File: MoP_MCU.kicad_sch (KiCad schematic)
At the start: 4 parts, among them J3 CN7, J4 CN10

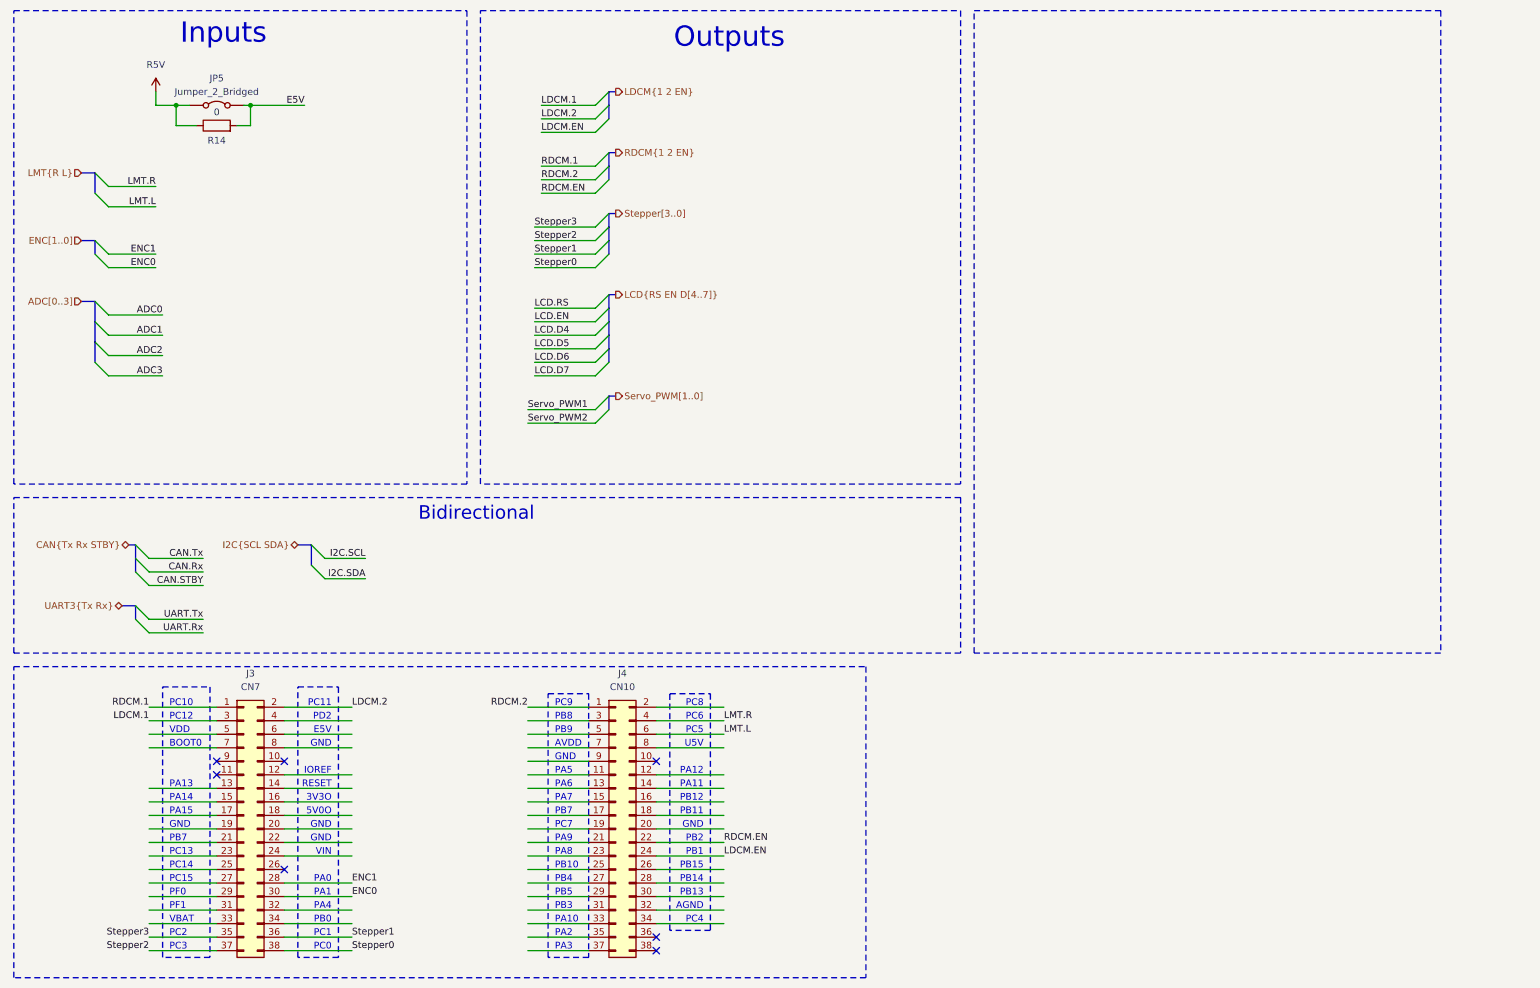
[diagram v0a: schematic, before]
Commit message: changed ref designators to be consistent accross sheets
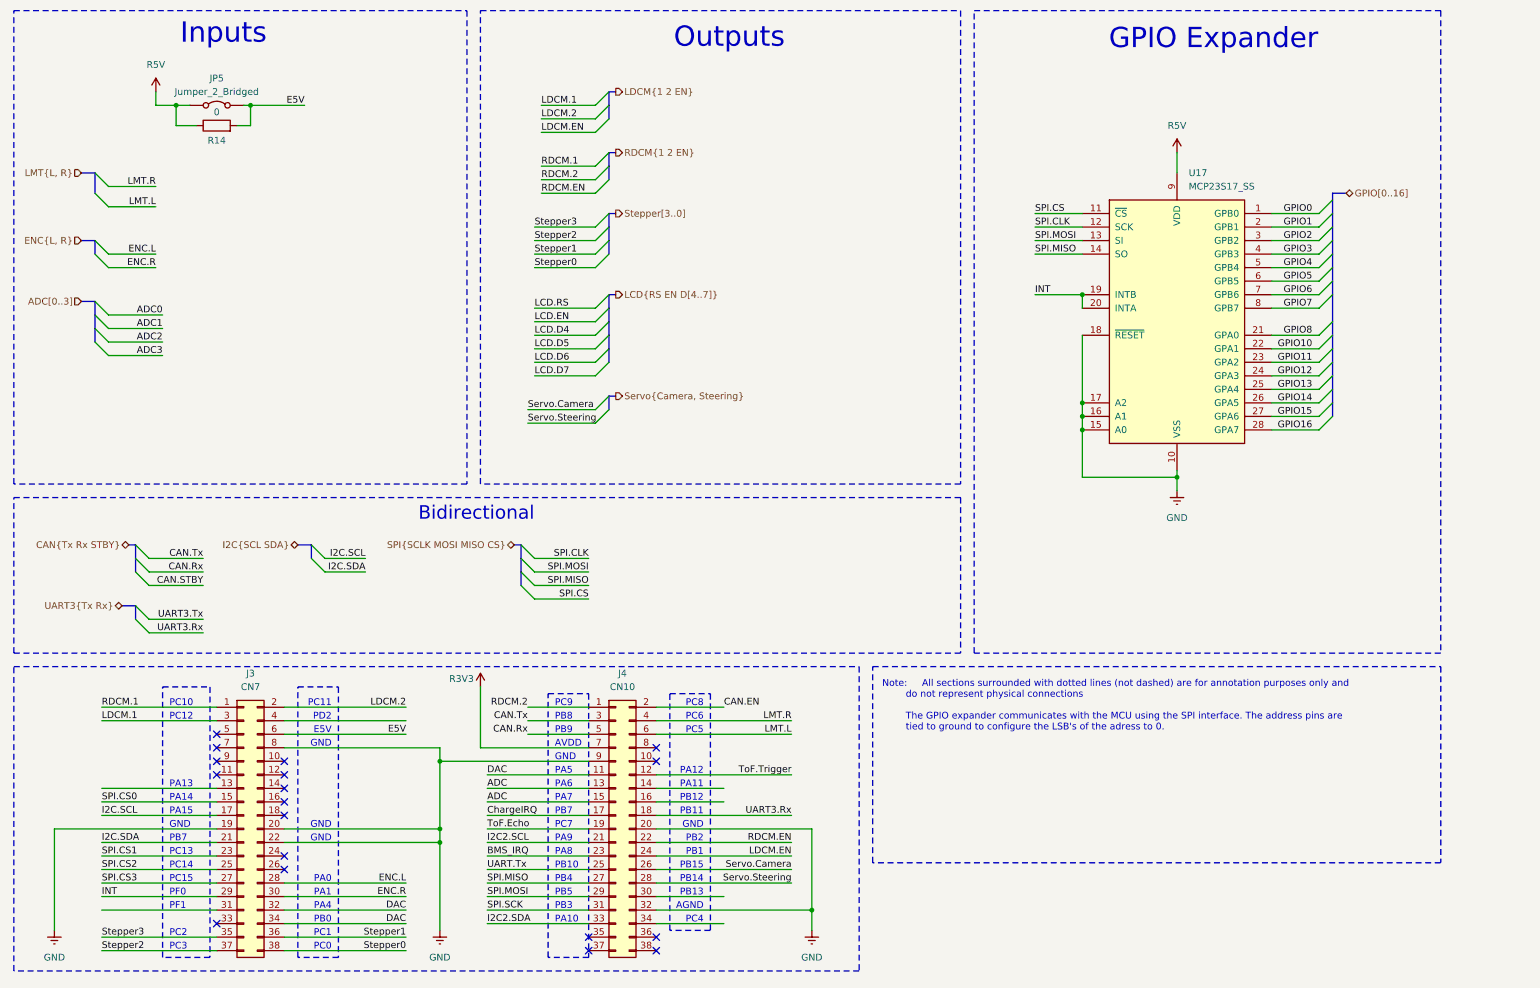
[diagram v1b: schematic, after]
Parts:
- added U17: MCP23S17_SS, Package_SO:SSOP-28_5.3x10.2mm_P0.65mm, symbol Interface_Expansion:MCP23S17_SS
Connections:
- net CAN.Rx: now also J4.5 (Pin_5)
- net CAN.Tx: now also J4.3 (Pin_3)
- net E5V: now also J3.6 (Pin_6)
- net I2C.SCL: now also J3.17 (Pin_17)
- net I2C.SDA: now also J3.21 (Pin_21)
- net R5V: now also U17.9 (VDD)
- net UART.Tx: now also J4.25 (Pin_25)
- net SPI.CS0: now reaches J3.15 (Pin_15)
- net GND: now reaches J3.19 (Pin_19)
- net GND: now also J3.20 (Pin_20), J3.22 (Pin_22), J3.8 (Pin_8), J4.20 (Pin_20), J4.32 (Pin_32), J4.9 (Pin_9), U17.10 (VSS), U17.15 (A0), U17.16 (A1), U17.17 (A2), U17.18 (~{RESET})
- net SPI.CS1: now reaches J3.23 (Pin_23)
- net SPI.CS2: now reaches J3.25 (Pin_25)
- net SPI.CS3: now reaches J3.27 (Pin_27)
- net INT: now reaches J3.29 (Pin_29)
- net INT: now also U17.19 (INTB), U17.20 (INTA)
- net DAC: now reaches J3.32 (Pin_32)
- net DAC: now also J3.34 (Pin_34), J4.11 (Pin_11)
- net ToF.Trigger: now reaches J4.12 (Pin_12)
- net ADC: now reaches J4.13 (Pin_13)
- net ADC: now also J4.15 (Pin_15)
- net ChargeIRQ: now reaches J4.17 (Pin_17)
- net UART3.Rx: now reaches J4.18 (Pin_18)
- net ToF.Echo: now reaches J4.19 (Pin_19)
- net CAN.EN: now reaches J4.2 (Pin_2)
- net I2C2.SCL: now reaches J4.21 (Pin_21)
- net BMS_IRQ: now reaches J4.23 (Pin_23)
- net Servo.Camera: now reaches J4.26 (Pin_26)
- net SPI.MISO: now reaches J4.27 (Pin_27)
- net SPI.MISO: now also U17.14 (SO)
- net Servo.Steering: now reaches J4.28 (Pin_28)
- net SPI.MOSI: now reaches J4.29 (Pin_29)
- net SPI.MOSI: now also U17.13 (SI)
- net SPI.SCK: now reaches J4.31 (Pin_31)
- net I2C2.SDA: now reaches J4.33 (Pin_33)
- net R3V3: now reaches J4.7 (Pin_7)
- net ENC0 renamed ENC.R
- net ENC1 renamed ENC.L
- new net GPIO0: U17.1 (GPB0)
- new net GPIO1: U17.2 (GPB1)
- new net GPIO10: U17.22 (GPA1)
- new net GPIO11: U17.23 (GPA2)
- new net GPIO12: U17.24 (GPA3)
- new net GPIO13: U17.25 (GPA4)
- new net GPIO14: U17.26 (GPA5)
- new net GPIO15: U17.27 (GPA6)
- new net GPIO16: U17.28 (GPA7)
- new net GPIO2: U17.3 (GPB2)
- new net GPIO3: U17.4 (GPB3)
- new net GPIO4: U17.5 (GPB4)
- new net GPIO5: U17.6 (GPB5)
- new net GPIO6: U17.7 (GPB6)
- new net GPIO7: U17.8 (GPB7)
- new net GPIO8: U17.21 (GPA0)
- new net SPI.CLK: U17.12 (SCK)
- new net SPI.CS: U17.11 (~{CS})
- no-connect marks 7 -> 18
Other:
- note added: "GPIO Expander"
- note added: "Note: All sections surrounded with dotted lines (not dashed) are for annotation purposes only and do not represent physical connections The GPIO expander communicates with the MCU using the SPI interface. The address pins are tied to ground to configure the LSB's of the adress to 0."
- note removed: "3V3O"
- note removed: "5V0O"
- note removed: "BOOT0"
- note removed: "IOREF"
- note removed: "PA2"
- note removed: "PA3"
- note removed: "RESET"
- note removed: "U5V"
- note removed: "VBAT"
- note removed: "VDD"
- note removed: "VIN"

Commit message: Finished schematics
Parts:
- J1201: renamed from J3; footprint (none) -> Connector_PinHeader_2.54mm:PinHeader_2x19_P2.54mm_Vertical
- J1202: renamed from J4; footprint (none) -> Connector_PinHeader_2.54mm:PinHeader_2x19_P2.54mm_Vertical
- JP1201: renamed from JP5; footprint (none) -> Connector_PinHeader_2.54mm:PinHeader_1x02_P2.54mm_Vertical
- R1201: renamed from R14; footprint (none) -> Resistor_SMD:R_0805_2012Metric
- renumbered U17 to U1201
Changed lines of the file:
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@@
+	(wire
+		(pts
+			(xy 76.2 49.53) (xy 88.9 49.53)
+		)
+		(stroke
+			(width 0)
+			(type default)
+		)
+	)
 	(wire
 		(pts
@@
 		)
 	)
+	(wire
+		(pts
+			(xy 76.2 45.72) (xy 88.9 45.72)
+		)
+		(stroke
+			(width 0)
+			(type default)
+		)
+	)
 	(bus
 		(pts
@@
 		)
 	)
+	(label "Alert"
+		(at 88.9 49.53 180)
+		(fields_autoplaced yes)
+		(effects
+			(font
+				(size 1.27 1.27)
+			)
+			(justify right bottom)
+		)
+	)
 	(label "ADC2"
 		(at 43.18 77.47 180)
@@
 	(label "CAN.Rx"
 		(at 111.76 151.13 180)
+		(fields_autoplaced yes)
+		(effects
+			(font
+				(size 1.27 1.27)
+			)
+			(justify right bottom)
+		)
+	)
+	(label "~{PROCHOT}"
+		(at 88.9 45.72 180)
 		(fields_autoplaced yes)
 		(effects
@@
 		)
 	)
+	(hierarchical_label "Alert"
+		(shape input)
+		(at 76.2 49.53 180)
+		(fields_autoplaced yes)
+		(effects
+			(font
+				(size 1.27 1.27)
+			)
+			(justify right)
+		)
+	)
 	(hierarchical_label "UART3{Tx Rx}"
 		(shape bidirectional)
@@
 		(shape input)
 		(at 27.94 58.42 180)
+		(fields_autoplaced yes)
+		(effects
+			(font
+				(size 1.27 1.27)
+			)
+			(justify right)
+		)
+	)
+	(hierarchical_label "~{PROCHOT}"
+		(shape input)
+		(at 76.2 45.72 180)
 		(fields_autoplaced yes)
 		(effects
@@
 		(on_board yes)
 		(dnp no)
-		(property "Reference" "R14"
+		(property "Reference" "R1201"
 			(at 53.34 39.624 90)
 			(effects
@@
 			)
 		)
-		(property "Footprint" ""
+		(property "Footprint" "Resistor_SMD:R_0805_2012Metric"
 			(at 53.34 38.608 90)
 			(effects
@@
 			(project ""
 				(path "/4d76798e-9a11-4d8d-a723-72f274a89091/776889f8-2577-4d11-8ed0-968f1ffe11b5"
-					(reference "R14")
+					(reference "R1201")
 					(unit 1)
 				)
@@
 		(on_board yes)
 		(dnp no)
-		(fields_autoplaced yes)
-		(property "Reference" "JP5"
-			(at 53.34 27.94 0)
+		(property "Reference" "JP1201"
+			(at 53.34 30.734 0)
 			(effects
 				(font
@@
 					(size 1.27 1.27)
 				)
-			)
-		)
-		(property "Footprint" ""
+				(hide yes)
+			)
+		)
+		(property "Footprint" "Connector_PinHeader_2.54mm:PinHeader_1x02_P2.54mm_Vertical"
 			(at 53.34 33.02 0)
 			(effects
@@
 			(project ""
 				(path "/4d76798e-9a11-4d8d-a723-72f274a89091/776889f8-2577-4d11-8ed0-968f1ffe11b5"
-					(reference "JP5")
+					(reference "JP1201")
 					(unit 1)
 				)
@@
 		(dnp no)
 		(fields_autoplaced yes)
-		(property "Reference" "U17"
+		(property "Reference" "U1201"
 			(at 235.8741 45.72 0)
 			(effects
@@
 			(project ""
 				(path "/4d76798e-9a11-4d8d-a723-72f274a89091/776889f8-2577-4d11-8ed0-968f1ffe11b5"
-					(reference "U17")
+					(reference "U1201")
 					(unit 1)
 				)
@@
 		(dnp no)
 		(fields_autoplaced yes)
-		(property "Reference" "J3"
+		(property "Reference" "J1201"
 			(at 59.69 139.7 0)
 			(effects
@@
 			)
 		)
-		(property "Footprint" ""
+		(property "Footprint" "Connector_PinHeader_2.54mm:PinHeader_2x19_P2.54mm_Vertical"
 			(at 58.42 168.91 0)
 			(effects
@@
 			(project "MoP"
 				(path "/4d76798e-9a11-4d8d-a723-72f274a89091/776889f8-2577-4d11-8ed0-968f1ffe11b5"
-					(reference "J3")
+					(reference "J1201")
 					(unit 1)
 				)
@@
 		(dnp no)
 		(fields_autoplaced yes)
-		(property "Reference" "J4"
+		(property "Reference" "J1202"
 			(at 129.54 139.7 0)
 			(effects
@@
 			)
 		)
-		(property "Footprint" ""
+		(property "Footprint" "Connector_PinHeader_2.54mm:PinHeader_2x19_P2.54mm_Vertical"
 			(at 128.27 168.91 0)
 			(effects
@@
 			(project "MoP"
 				(path "/4d76798e-9a11-4d8d-a723-72f274a89091/776889f8-2577-4d11-8ed0-968f1ffe11b5"
-					(reference "J4")
+					(reference "J1202")
 					(unit 1)
 				)

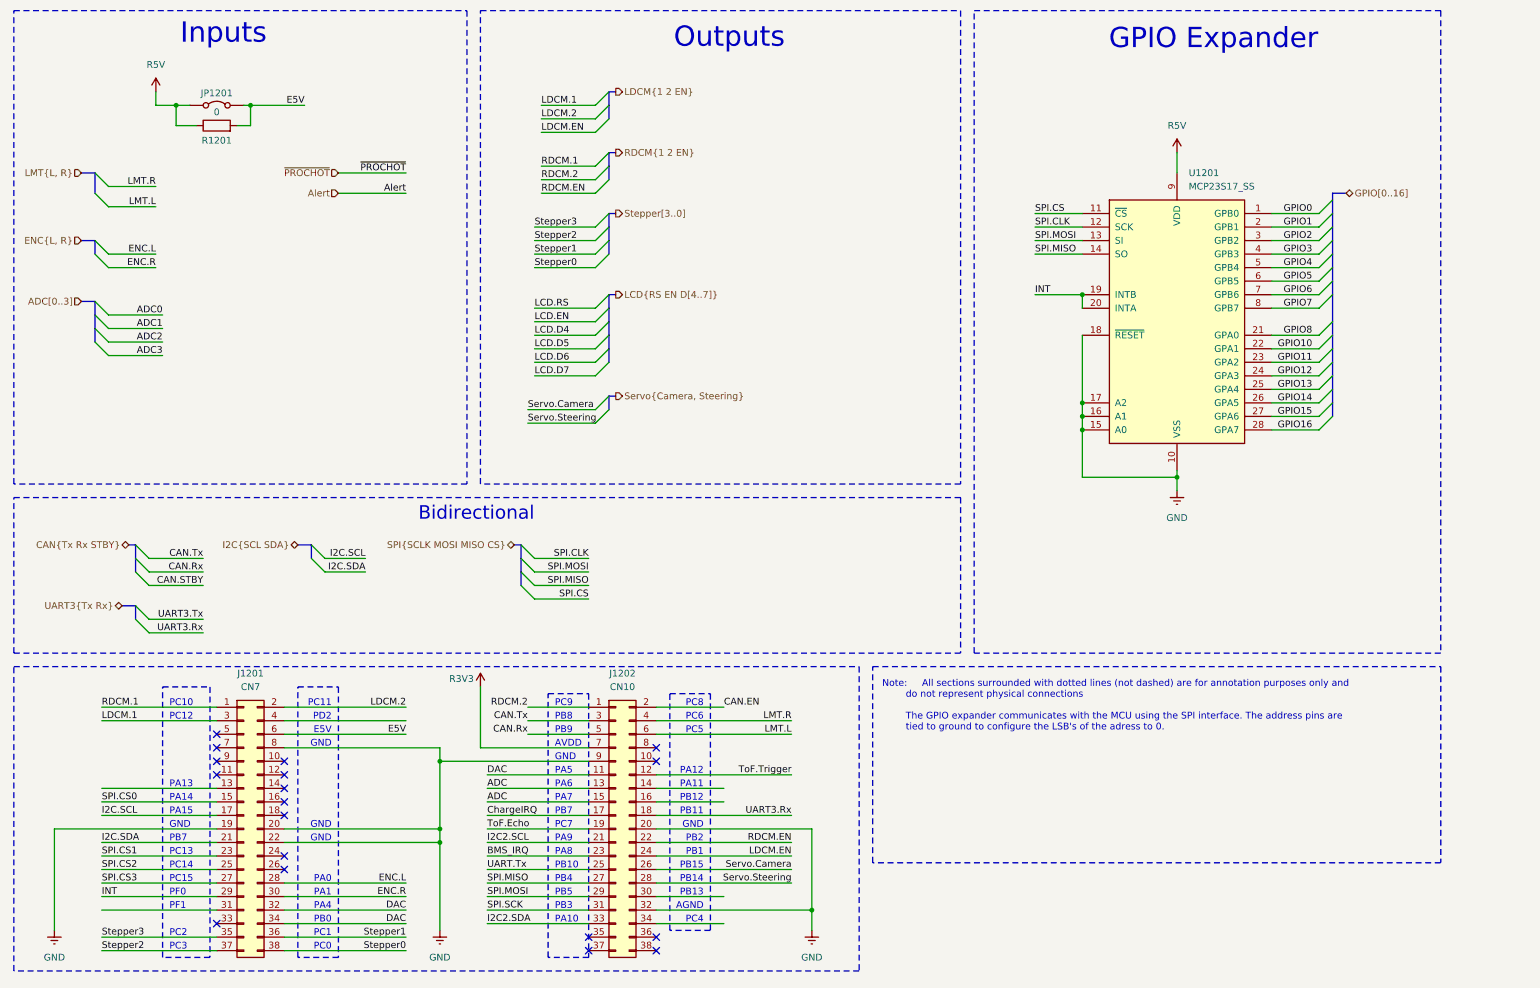
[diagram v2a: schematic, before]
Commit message: Added subproject for EPS PCB
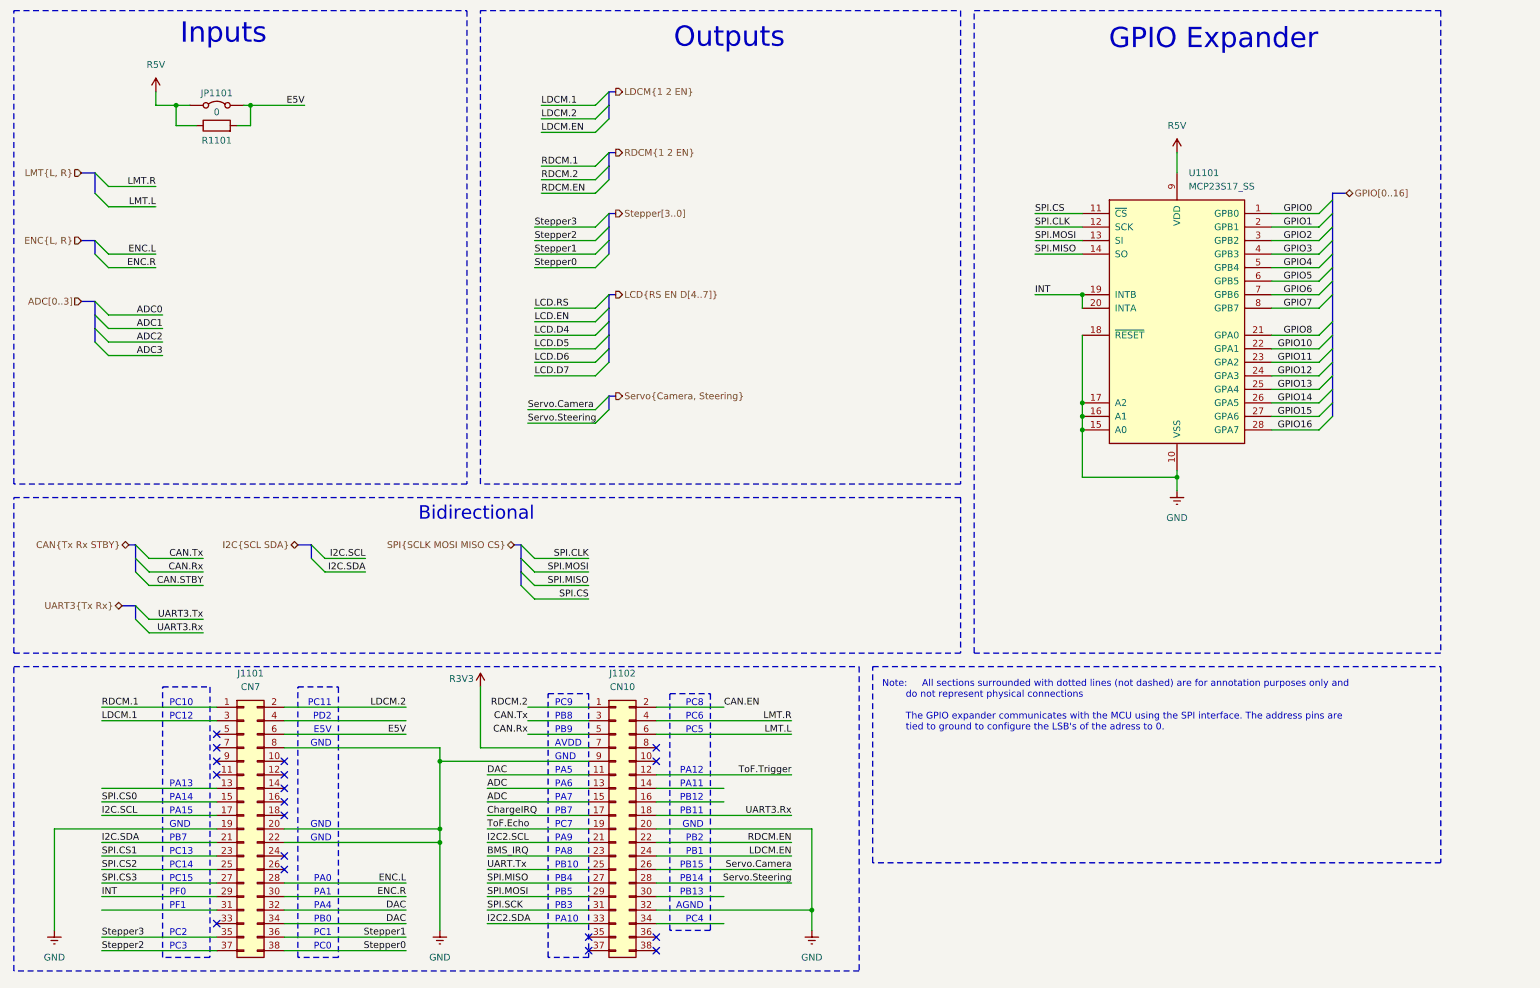
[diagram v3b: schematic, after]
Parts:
- renumbered J1201 to J1101, J1202 to J1102, JP1201 to JP1101, R1201 to R1101, U1201 to U1101

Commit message: added OBC
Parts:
- R1101: now not fitted
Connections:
- net CAN.EN is gone; now on net CAN.STBY: J1102.2 (Pin_2)
- net ChargeIRQ is gone; now on net ADC2: J1102.17 (Pin_17)
- net GPIO11 is gone; now on net LCD.RS: U1101.23 (GPA2)
- net GPIO12 is gone; now on net LCD.EN: U1101.24 (GPA3)
- net GPIO13 is gone; now on net LCD.D4: U1101.25 (GPA4)
- net GPIO14 is gone; now on net LCD.D5: U1101.26 (GPA5)
- net GPIO15 is gone; now on net LCD.D6: U1101.27 (GPA6)
- net GPIO16 is gone; now on net LCD.D7: U1101.28 (GPA7)
- net SPI.CLK is gone; now on net SPI.SCK: U1101.12 (SCK)
- net SPI.CS is gone; now on net SPI.CS0: U1101.11 (~{CS})
- net UART.Tx is gone; now on net UART3.Tx: J1102.25 (Pin_25)
- net ADC0: now also J1102.13 (Pin_13)
- net ADC1: now also J1102.15 (Pin_15)
- net Keypad0: now reaches J1101.13 (Pin_13)
- net Keypad1: now reaches J1101.31 (Pin_31)
- net Keypad2: now reaches J1101.4 (Pin_4)
- net Keypad4: now reaches J1102.14 (Pin_14)
- net Keypad5: now reaches J1102.16 (Pin_16)
- net Keypad6: now reaches J1102.30 (Pin_30)
- net Keypad7: now reaches J1102.34 (Pin_34)
- removed net ADC: J1102.13 (Pin_13), J1102.15 (Pin_15)
- net BMS_IRQ renamed Keypad3
- removed net DAC: J1101.32 (Pin_32), J1101.34 (Pin_34), J1102.11 (Pin_11)
- net GPIO10 renamed GPIO9
- net R3V3: no longer names the net of J1102.7 (Pin_7)
- new net DAC0: J1101.32 (Pin_32)
- new net DAC1: J1101.34 (Pin_34)
- new net DAC2: J1102.11 (Pin_11)
- no-connect marks 18 -> 19
